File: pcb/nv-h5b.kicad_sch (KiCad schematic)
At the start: 17 parts, among them J1 PSH02-03, J2 Conn_01x01, J3 Conn_01x01, J4 Conn_01x01, J5 Conn_01x01, J6 Conn_01x01, J7 Conn_01x01, U1 ATtiny25-20SS

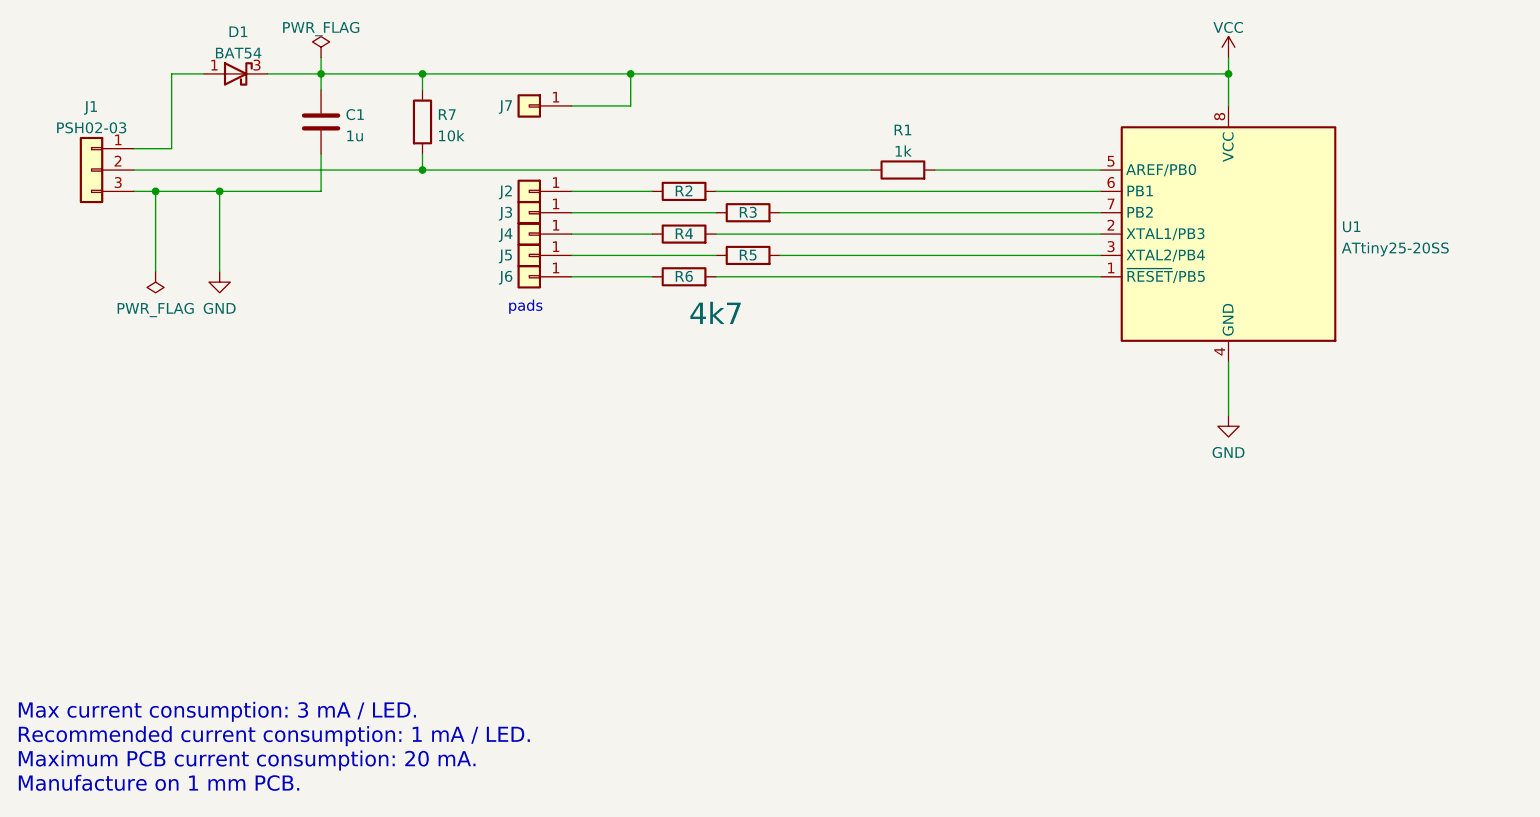
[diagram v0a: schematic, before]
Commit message: Route PCB.
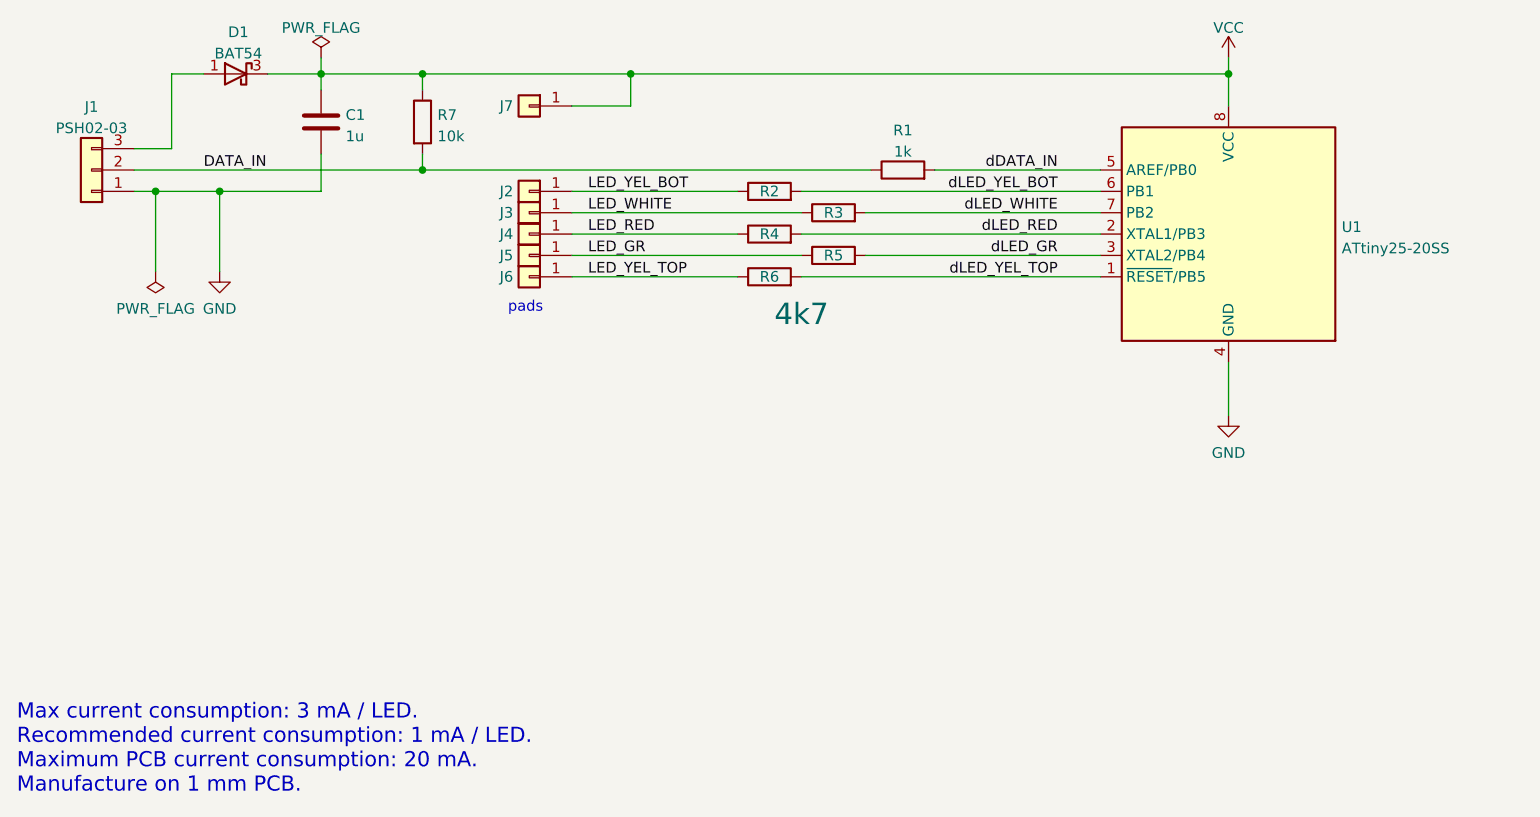
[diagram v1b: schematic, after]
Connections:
- net GND: now also J1.1 (Pin_1); no longer J1.3 (Pin_3)
- net DATA_IN: now reaches J1.2 (Pin_2), R1.1, R7.2
- net at D1.1 (A): now also J1.3 (Pin_3); no longer J1.1 (Pin_1)
- net dLED_YEL_TOP: now reaches R6.2, U1.1 (~{RESET}/PB5)
- net dLED_RED: now reaches R4.2, U1.2 (XTAL1/PB3)
- net dLED_GR: now reaches R5.2, U1.3 (XTAL2/PB4)
- net dDATA_IN: now reaches R1.2, U1.5 (AREF/PB0)
- net dLED_YEL_BOT: now reaches R2.2, U1.6 (PB1)
- net dLED_WHITE: now reaches R3.2, U1.7 (PB2)
- net LED_YEL_BOT: now reaches J2.1 (Pin_1), R2.1
- net LED_WHITE: now reaches J3.1 (Pin_1), R3.1
- net LED_GR: now reaches J5.1 (Pin_1), R5.1
- net LED_RED: now reaches J4.1 (Pin_1), R4.1
- net LED_YEL_TOP: now reaches J6.1 (Pin_1), R6.1
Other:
- moved on the sheet: J1, R2, R3, R4, R5, R6
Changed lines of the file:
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@@
     (stroke (width 0) (type default) (color 0 0 0 0))
   )
-  (wire (pts (xy 83.185 57.15) (xy 92.71 57.15))
+  (wire (pts (xy 83.185 57.15) (xy 102.87 57.15))
     (stroke (width 0) (type default) (color 0 0 0 0))
   )
@@
     (stroke (width 0) (type default) (color 0 0 0 0))
   )
-  (wire (pts (xy 83.185 52.07) (xy 92.71 52.07))
+  (wire (pts (xy 83.185 52.07) (xy 102.87 52.07))
     (stroke (width 0) (type default) (color 0 0 0 0))
   )
@@
     (stroke (width 0) (type default) (color 0 0 0 0))
   )
-  (wire (pts (xy 107.95 59.69) (xy 146.05 59.69))
-    (stroke (width 0) (type default) (color 0 0 0 0))
-  )
-  (wire (pts (xy 100.33 52.07) (xy 146.05 52.07))
+  (wire (pts (xy 118.11 59.69) (xy 146.05 59.69))
     (stroke (width 0) (type default) (color 0 0 0 0))
   )
@@
     (stroke (width 0) (type default) (color 0 0 0 0))
   )
-  (wire (pts (xy 83.185 54.61) (xy 100.33 54.61))
-    (stroke (width 0) (type default) (color 0 0 0 0))
-  )
-  (wire (pts (xy 107.95 54.61) (xy 146.05 54.61))
+  (wire (pts (xy 83.185 54.61) (xy 110.49 54.61))
     (stroke (width 0) (type default) (color 0 0 0 0))
   )
@@
     (stroke (width 0) (type default) (color 0 0 0 0))
   )
-  (wire (pts (xy 100.33 62.23) (xy 146.05 62.23))
-    (stroke (width 0) (type default) (color 0 0 0 0))
-  )
-  (wire (pts (xy 83.185 62.23) (xy 92.71 62.23))
+  (wire (pts (xy 83.185 62.23) (xy 102.87 62.23))
     (stroke (width 0) (type default) (color 0 0 0 0))
   )
@@
     (stroke (width 0) (type default) (color 0 0 0 0))
   )
+  (wire (pts (xy 110.49 57.15) (xy 146.05 57.15))
+    (stroke (width 0) (type default) (color 0 0 0 0))
+  )
   (wire (pts (xy 35.56 46.99) (xy 35.56 38.1))
     (stroke (width 0) (type default) (color 0 0 0 0))
@@
     (stroke (width 0) (type default) (color 0 0 0 0))
   )
-  (wire (pts (xy 83.185 59.69) (xy 100.33 59.69))
+  (wire (pts (xy 118.11 54.61) (xy 146.05 54.61))
+    (stroke (width 0) (type default) (color 0 0 0 0))
+  )
+  (wire (pts (xy 83.185 59.69) (xy 110.49 59.69))
     (stroke (width 0) (type default) (color 0 0 0 0))
   )
@@
     (stroke (width 0) (type default) (color 0 0 0 0))
   )
-  (wire (pts (xy 100.33 57.15) (xy 146.05 57.15))
-    (stroke (width 0) (type default) (color 0 0 0 0))
-  )
   (wire (pts (xy 65.405 38.1) (xy 90.17 38.1))
     (stroke (width 0) (type default) (color 0 0 0 0))
   )
+  (wire (pts (xy 110.49 52.07) (xy 146.05 52.07))
+    (stroke (width 0) (type default) (color 0 0 0 0))
+  )
   (wire (pts (xy 35.56 38.1) (xy 39.37 38.1))
     (stroke (width 0) (type default) (color 0 0 0 0))
@@
   )
   (wire (pts (xy 65.405 38.1) (xy 65.405 40.005))
+    (stroke (width 0) (type default) (color 0 0 0 0))
+  )
+  (wire (pts (xy 110.49 62.23) (xy 146.05 62.23))
     (stroke (width 0) (type default) (color 0 0 0 0))
   )
@@
     (effects (font (size 1.27 1.27)) (justify left bottom))
   )
+  (label "dLED_WHITE" (at 140.97 54.61 180)
+    (effects (font (size 1.27 1.27)) (justify right bottom))
+  )
+  (label "LED_YEL_BOT" (at 85.09 52.07 0)
+    (effects (font (size 1.27 1.27)) (justify left bottom))
+  )
+  (label "DATA_IN" (at 39.37 49.53 0)
+    (effects (font (size 1.27 1.27)) (justify left bottom))
+  )
+  (label "dLED_YEL_TOP" (at 140.97 62.23 180)
+    (effects (font (size 1.27 1.27)) (justify right bottom))
+  )
+  (label "dLED_GR" (at 140.97 59.69 180)
+    (effects (font (size 1.27 1.27)) (justify right bottom))
+  )
+  (label "dDATA_IN" (at 140.97 49.53 180)
+    (effects (font (size 1.27 1.27)) (justify right bottom))
+  )
+  (label "LED_WHITE" (at 85.09 54.61 0)
+    (effects (font (size 1.27 1.27)) (justify left bottom))
+  )
+  (label "LED_GR" (at 85.09 59.69 0)
+    (effects (font (size 1.27 1.27)) (justify left bottom))
+  )
+  (label "LED_YEL_TOP" (at 85.09 62.23 0)
+    (effects (font (size 1.27 1.27)) (justify left bottom))
+  )
+  (label "LED_RED" (at 85.09 57.15 0)
+    (effects (font (size 1.27 1.27)) (justify left bottom))
+  )
+  (label "dLED_RED" (at 140.97 57.15 180)
+    (effects (font (size 1.27 1.27)) (justify right bottom))
+  )
+  (label "dLED_YEL_BOT" (at 140.97 52.07 180)
+    (effects (font (size 1.27 1.27)) (justify right bottom))
+  )
   (symbol (lib_id "Device:R") (at 65.405 43.815 0) (unit 1)
     (in_bom yes) (on_board yes) (fields_autoplaced)
@@
     (pin "2")
   )
-  (symbol (lib_id "Connector_Generic:Conn_01x03") (at 26.035 49.53 0) (mirror y) (unit 1)
+  (symbol (lib_id "Connector_Generic:Conn_01x03") (at 26.035 49.53 180) (unit 1)
     (in_bom yes) (on_board yes) (fields_autoplaced)
     (property "Reference" "J1" (id 0) (at 26.035 42.0202 0))
@@
     (pin "1")
   )
-  (symbol (lib_id "Device:R") (at 104.14 54.61 90) (unit 1)
-    (in_bom yes) (on_board yes)
-    (property "Reference" "R3" (id 0) (at 104.14 54.61 90))
-    (property "Value" "4k7" (id 1) (at 104.14 52.4311 90)
-      (effects (font (size 1.27 1.27)) hide)
-    )
-    (property "Footprint" "Resistor_SMD:R_0805_2012Metric" (id 2) (at 104.14 56.388 90)
-      (effects (font (size 1.27 1.27)) hide)
-    )
-    (property "Datasheet" "~" (id 3) (at 104.14 54.61 0)
+  (symbol (lib_id "Device:R") (at 114.3 54.61 90) (unit 1)
+    (in_bom yes) (on_board yes)
+    (property "Reference" "R3" (id 0) (at 114.3 54.61 90))
+    (property "Value" "4k7" (id 1) (at 114.3 52.4311 90)
+      (effects (font (size 1.27 1.27)) hide)
+    )
+    (property "Footprint" "Resistor_SMD:R_0805_2012Metric" (id 2) (at 114.3 56.388 90)
+      (effects (font (size 1.27 1.27)) hide)
+    )
+    (property "Datasheet" "~" (id 3) (at 114.3 54.61 0)
       (effects (font (size 1.27 1.27)) hide)
     )
@@
     (pin "1")
   )
-  (symbol (lib_id "Device:R") (at 96.52 57.15 90) (unit 1)
-    (in_bom yes) (on_board yes)
-    (property "Reference" "R4" (id 0) (at 96.52 57.15 90))
-    (property "Value" "4k7" (id 1) (at 96.52 54.9711 90)
-      (effects (font (size 1.27 1.27)) hide)
-    )
-    (property "Footprint" "Resistor_SMD:R_0805_2012Metric" (id 2) (at 96.52 58.928 90)
-      (effects (font (size 1.27 1.27)) hide)
-    )
-    (property "Datasheet" "~" (id 3) (at 96.52 57.15 0)
-      (effects (font (size 1.27 1.27)) hide)
-    )
-    (pin "1")
-    (pin "2")
-  )
-  (symbol (lib_id "Device:R") (at 96.52 52.07 90) (unit 1)
-    (in_bom yes) (on_board yes)
-    (property "Reference" "R2" (id 0) (at 96.52 52.07 90))
-    (property "Value" "4k7" (id 1) (at 100.33 66.675 90)
+  (symbol (lib_id "Device:R") (at 106.68 57.15 90) (unit 1)
+    (in_bom yes) (on_board yes)
+    (property "Reference" "R4" (id 0) (at 106.68 57.15 90))
+    (property "Value" "4k7" (id 1) (at 106.68 54.9711 90)
+      (effects (font (size 1.27 1.27)) hide)
+    )
+    (property "Footprint" "Resistor_SMD:R_0805_2012Metric" (id 2) (at 106.68 58.928 90)
+      (effects (font (size 1.27 1.27)) hide)
+    )
+    (property "Datasheet" "~" (id 3) (at 106.68 57.15 0)
+      (effects (font (size 1.27 1.27)) hide)
+    )
+    (pin "1")
+    (pin "2")
+  )
+  (symbol (lib_id "Device:R") (at 106.68 52.07 90) (unit 1)
+    (in_bom yes) (on_board yes)
+    (property "Reference" "R2" (id 0) (at 106.68 52.07 90))
+    (property "Value" "4k7" (id 1) (at 110.49 66.675 90)
       (effects (font (size 2.54 2.54)))
     )
-    (property "Footprint" "Resistor_SMD:R_0805_2012Metric" (id 2) (at 96.52 53.848 90)
-      (effects (font (size 1.27 1.27)) hide)
-    )
-    (property "Datasheet" "~" (id 3) (at 96.52 52.07 0)
-      (effects (font (size 1.27 1.27)) hide)
-    )
-    (pin "1")
-    (pin "2")
-  )
-  (symbol (lib_id "Device:R") (at 96.52 62.23 90) (unit 1)
-    (in_bom yes) (on_board yes)
-    (property "Reference" "R6" (id 0) (at 96.52 62.23 90))
-    (property "Value" "4k7" (id 1) (at 96.52 60.0511 90)
-      (effects (font (size 1.27 1.27)) hide)
-    )
-    (property "Footprint" "Resistor_SMD:R_0805_2012Metric" (id 2) (at 96.52 64.008 90)
-      (effects (font (size 1.27 1.27)) hide)
-    )
-    (property "Datasheet" "~" (id 3) (at 96.52 62.23 0)
+    (property "Footprint" "Resistor_SMD:R_0805_2012Metric" (id 2) (at 106.68 53.848 90)
+      (effects (font (size 1.27 1.27)) hide)
+    )
+    (property "Datasheet" "~" (id 3) (at 106.68 52.07 0)
+      (effects (font (size 1.27 1.27)) hide)
+    )
+    (pin "1")
+    (pin "2")
+  )
+  (symbol (lib_id "Device:R") (at 106.68 62.23 90) (unit 1)
+    (in_bom yes) (on_board yes)
+    (property "Reference" "R6" (id 0) (at 106.68 62.23 90))
+    (property "Value" "4k7" (id 1) (at 106.68 60.0511 90)
+      (effects (font (size 1.27 1.27)) hide)
+    )
+    (property "Footprint" "Resistor_SMD:R_0805_2012Metric" (id 2) (at 106.68 64.008 90)
+      (effects (font (size 1.27 1.27)) hide)
+    )
+    (property "Datasheet" "~" (id 3) (at 106.68 62.23 0)
       (effects (font (size 1.27 1.27)) hide)
     )
@@
     (pin "1")
   )
-  (symbol (lib_id "Device:R") (at 104.14 59.69 90) (unit 1)
-    (in_bom yes) (on_board yes)
-    (property "Reference" "R5" (id 0) (at 104.14 59.69 90))
-    (property "Value" "4k7" (id 1) (at 104.14 57.5111 90)
-      (effects (font (size 1.27 1.27)) hide)
-    )
-    (property "Footprint" "Resistor_SMD:R_0805_2012Metric" (id 2) (at 104.14 61.468 90)
-      (effects (font (size 1.27 1.27)) hide)
-    )
-    (property "Datasheet" "~" (id 3) (at 104.14 59.69 0)
-      (effects (font (size 1.27 1.27)) hide)
-    )
+  (symbol (lib_id "Device:R") (at 114.3 59.69 90) (unit 1)
+    (in_bom yes) (on_board yes)
+    (property "Reference" "R5" (id 0) (at 114.3 59.69 90))
+    (property "Value" "4k7" (id 1) (at 114.3 57.5111 90)
+      (effects (font (size 1.27 1.27)) hide)
+    )
+    (property "Footprint" "Resistor_SMD:R_0805_2012Metric" (id 2) (at 114.3 61.468 90)
+      (effects (font (size 1.27 1.27)) hide)
+    )
+    (property "Datasheet" "~" (id 3) (at 114.3 59.69 0)
+      (effects (font (size 1.27 1.27)) hide)
+    )

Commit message: Note possible alterantive versions of MCU.
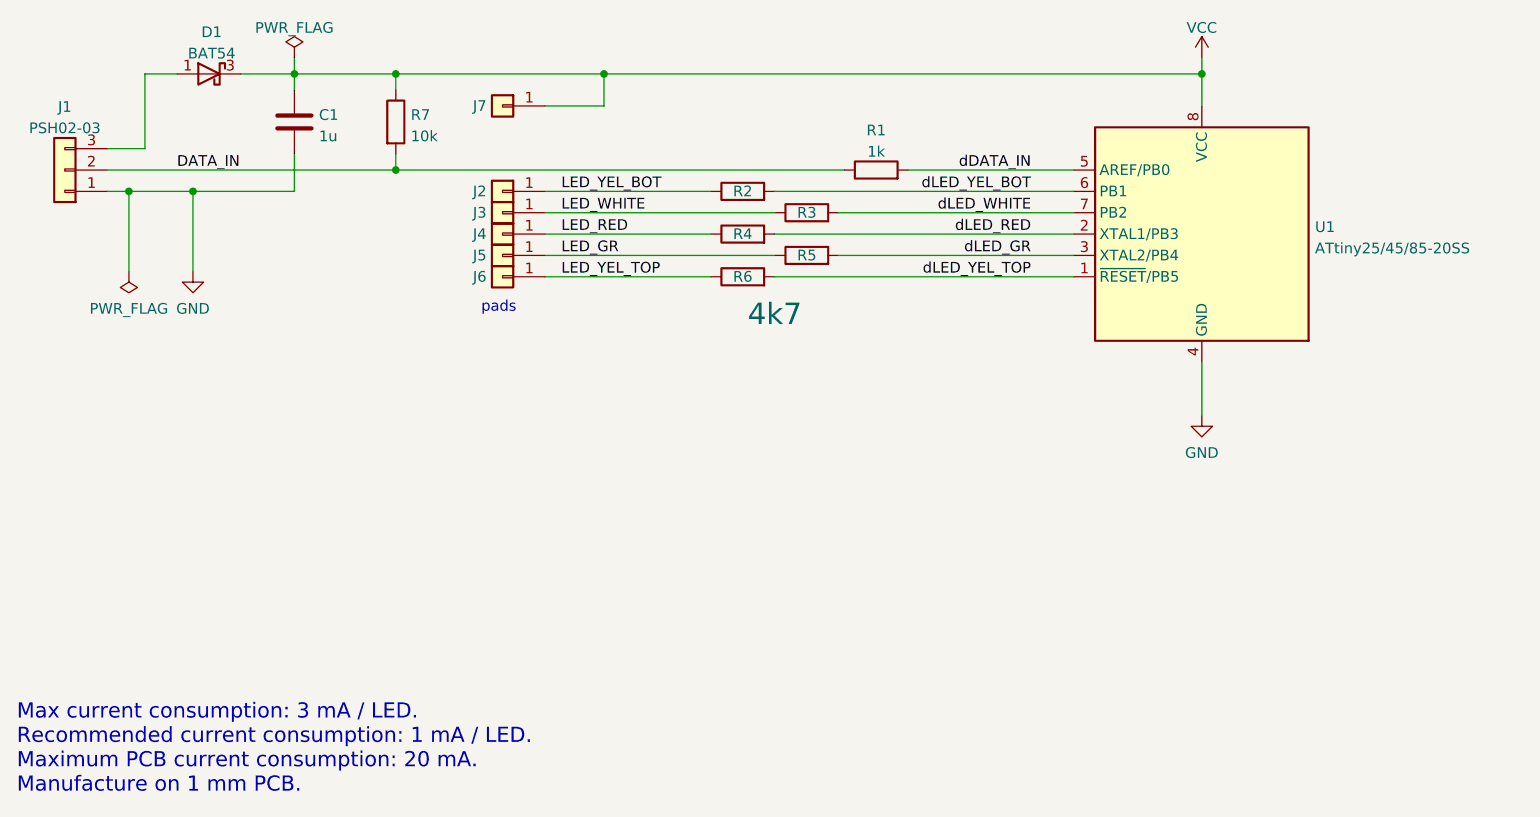
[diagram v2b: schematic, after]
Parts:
- U1: value ATtiny25-20SS -> ATtiny25/45/85-20SS
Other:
- moved on the sheet: C1, D1, J1, J2, J3, J4, J5, J6, J7, R1, R2, R3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
